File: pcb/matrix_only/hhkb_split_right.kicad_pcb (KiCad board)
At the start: 2 copper layers, 173.7 x 97.4 mm, 83 parts, among them SW1 CPG151101S11-2, SW10 CPG151101S11-2, SW11 CPG151101S11-2, SW12 CPG151101S11-2, SW13 CPG151101S11-2, SW14 CPG151101S11-2, SW15 CPG151101S11-2, SW16 CPG151101S11-2, SW17 CPG151101S11-2, SW18 CPG151101S11-2, SW19 CPG151101S11-2, SW2 CPG151101S11-2, SW20 CPG151101S11-2, SW21 CPG151101S11-2, SW22 CPG151101S11-2, SW23 CPG151101S11-2, SW24 CPG151101S11-2, SW25 CPG151101S11-2, SW26 CPG151101S11-2, SW27 CPG151101S11-2, SW28 CPG151101S11-2, SW29 CPG151101S11-2, SW3 CPG151101S11-2, SW30 CPG151101S11-2, SW31 CPG151101S11-2, SW32 CPG151101S11-2, SW33 CPG151101S11-2, SW34 CPG151101S11-2, SW4 CPG151101S11-2, SW5 CPG151101S11-2, SW6 CPG151101S11-2, SW7 CPG151101S11-2, SW8 CPG151101S11-2, SW9 CPG151101S11-2, U1 74LVC595, U2 74LVC595

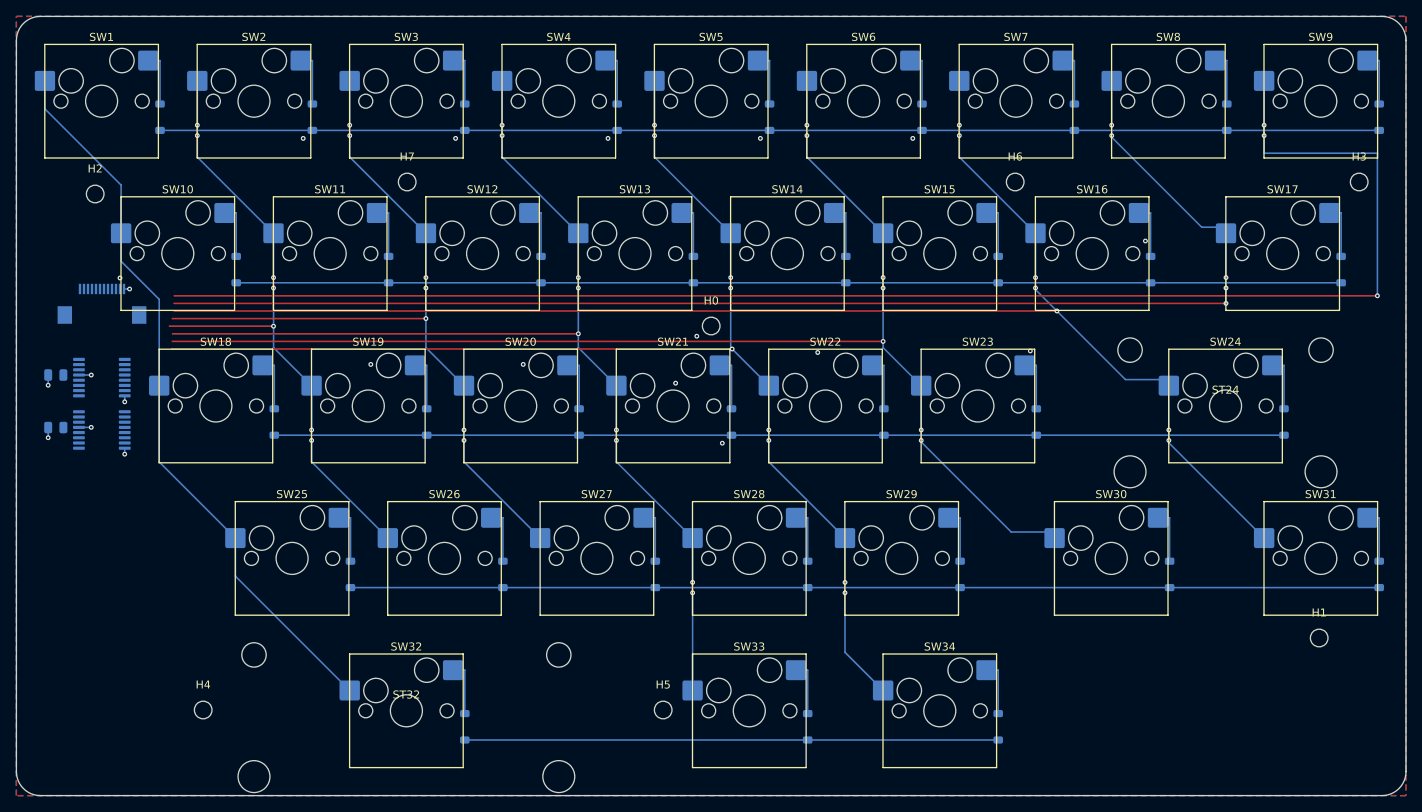
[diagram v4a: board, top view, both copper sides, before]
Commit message: 利用者が引いた配線を再現できるようにした（現物をスクリプト化）
利用者「**今の** matrix_only からスクリプト化すれば？」
「ただし、GND ベタ塗りとか、私が直せてないところは直してほしい」

## 仕組み

    tools/export_matrix_routing.py   pcb/matrix_only/ → pcb/matrix_routing.json
    tools/gen_pcb.py                 JSON を載せて pcb/unrouted/ へ

**規則として書き下すのではなく、現物の座標を写す。**私は規則を推測して
3 回失敗している（着地で U1 の他のパッドを横切る／レーンを縦に伸ばして
交差する／跨がない行に橋を架ける）。**利用者が引いた座標そのものが仕様。**

検証: 左 192 個・右 442 個が **0.002mm 以内で完全一致**（欠け 0）。

## 直したもの（利用者が直せていなかった部分）

1. **GND ベタが古かった。**`_pour` は配線を載せる前に走るので、あとから
   載る線を知らない。**最後に塗り直す**ようにした。
   `isolated_copper` 左 36 / 右 60 → **0**。離島も繋ぎ直した（左 9・右 16）。
2. **GND ビアが COL8 のレーンに乗っていた**（短絡 1・クリアランス 1）。
   `gnd_fanout.place` も配線より先に走るため。**当たるビアを外す処理**
   （`_drop_gnd_vias_hitting`）を足した。右 1 個 → 違反 0。

## 配置も取り込んだ

    U1   帯1 x=-62.787 dy=+1.375
    U2   帯1 x=-76.170 dy=+8.038 **角度 90**
    C_U1/C_U2  オフセットと**角度**（DECOUPLE_ANGLE を新設）

`_place_beside` は向きを自動で決めるが、利用者が IC を回した場合は
算出では出ないので、指定できるようにした。4 部品とも差 0.000mm。

## DRC

    左  違反 0 / 未配線 17（**左にはレーンが無い**——右だけ引かれている）
    右  dangling 9（レーン左端の余りと着地ビア）/ 未配線 **0**

短絡・交差・クリアランス・絶縁はすべて 0。

⚠️ **本番の pcb/ は触っていない**（利用者「まだ完成してないので、本番に
勝手にもっていかないでほしかった」）。

⚠️ `test_matrix_columns_do_not_need_long_crossings[right]` が新しく赤。
**利用者が引いたレーン（COL8 が 137.6mm の横断）を検出している。**
この検査は「列のバスに 27mm を超える区間があれば横断」と見るが、
**レーンは意図的な横断**なので前提が合わなくなった。別途直す。

Co-Authored-By: Claude Opus 5 (1M context) <noreply@anthropic.com>
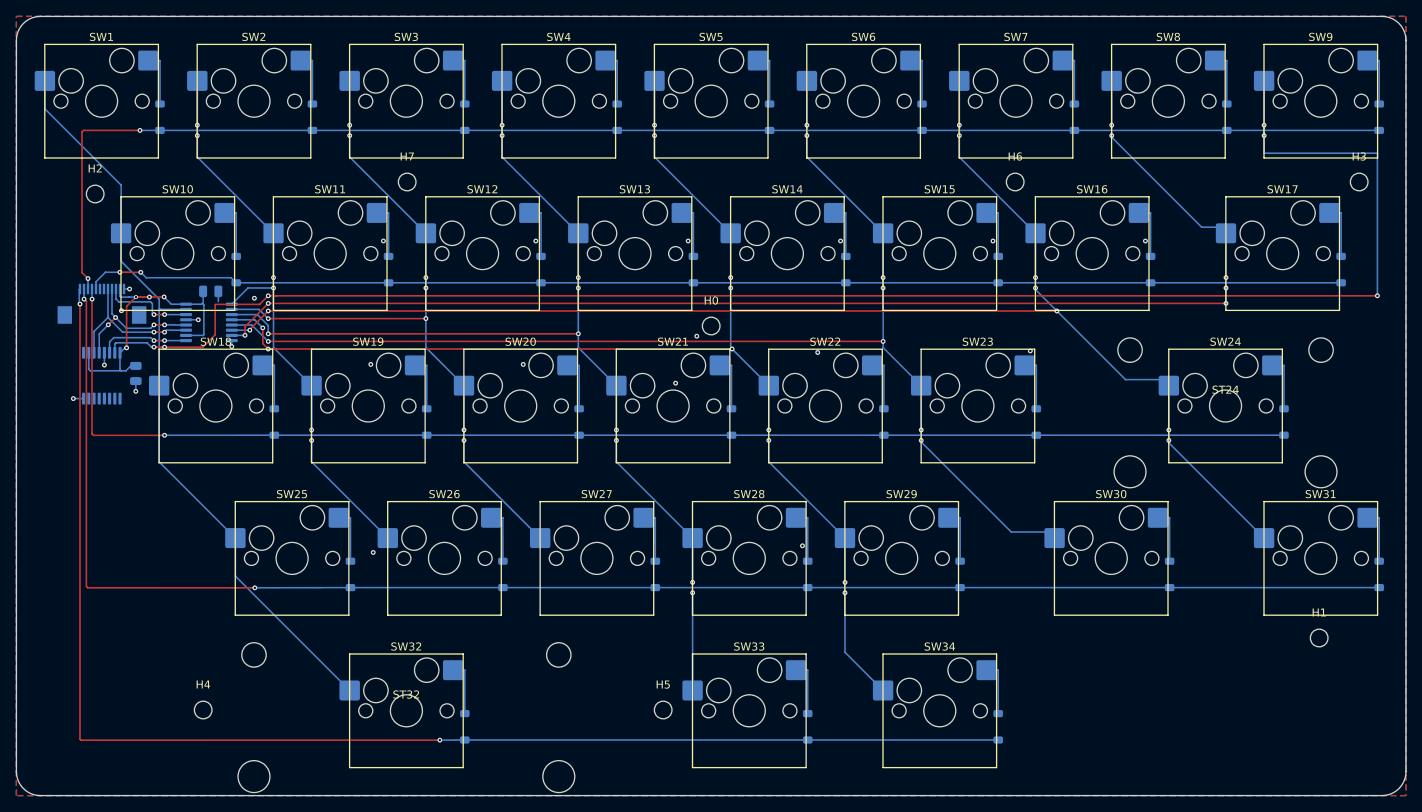
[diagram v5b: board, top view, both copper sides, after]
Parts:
- moved C_U1 22.0 mm to (87.4, 85.7), turned to 0 degrees
- moved U1 15.1 mm to (87.2, 89.5)
- moved C_U2 12.1 mm to (78.1, 95.9), turned to -90 degrees
- moved U2 6.78 mm to (73.8, 96.2), turned to 90 degrees
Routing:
- net ROW_E: track 66.7 -> 171.2 mm, vias 0 -> 2
- net ROW_D: track 128.6 -> 199.0 mm, vias 0 -> 2
- net ROW_B: track 126.2 -> 167.2 mm, vias 0 -> 2
- net V3V3: track 0.00 -> 39.7 mm, vias 1 -> 4
- net ROW_C: track 152.4 -> 182.2 mm, vias 0 -> 2
- net ROW_A: track 138.1 -> 157.7 mm, vias 0 -> 2
- net SPI_SCK: track 0.00 -> 19.3 mm, vias 0 -> 2
- net CS: track 0.00 -> 18.5 mm, vias 0 -> 4
- net COL8: track 191.4 -> 205.5 mm, vias 3 -> 6
- net SPI_MOSI: track 0.00 -> 11.6 mm, vias 0 -> 2
- net U1_U2: track 0.00 -> 11.3 mm, vias 0 -> 2
- net COL2: track 98.7 -> 91.8 mm, vias 7 -> 8
- net COL1: track 80.0 -> 73.1 mm, vias 7 -> 6
- net COL5: track 162.0 -> 155.4 mm, vias 7 -> 8
- net COL6: track 186.4 -> 180.3 mm, vias 7 -> 9
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
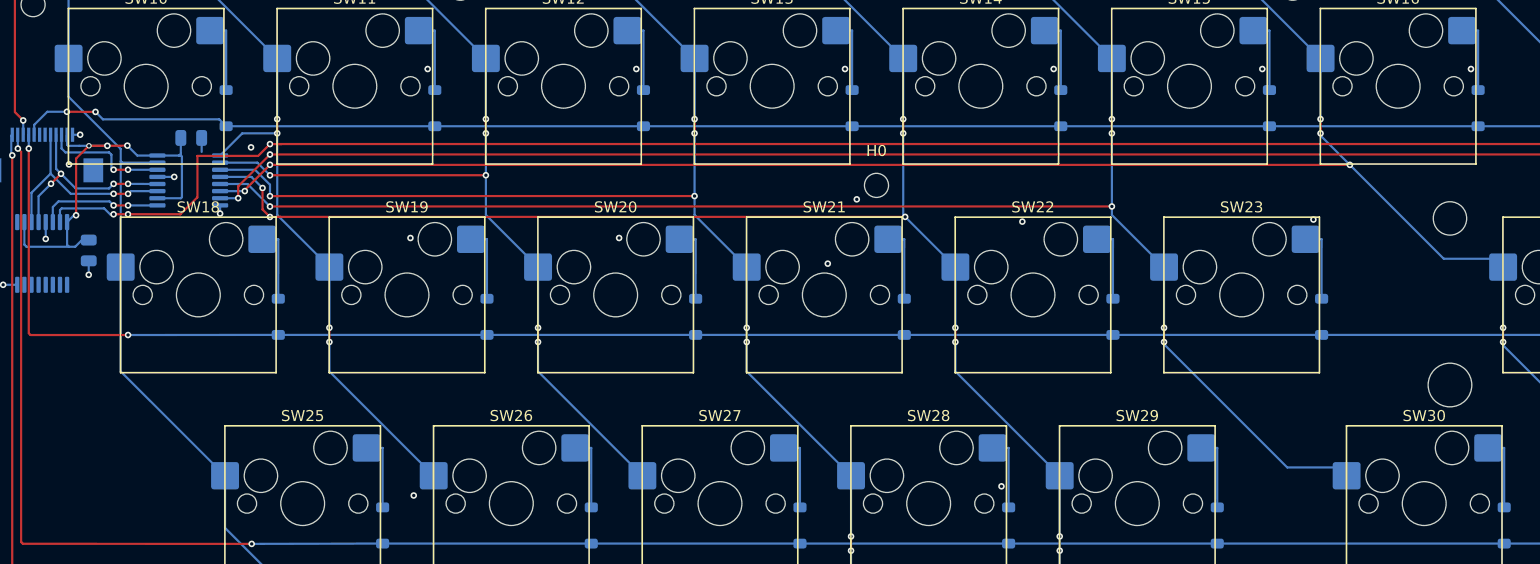
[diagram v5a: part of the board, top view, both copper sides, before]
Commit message: どこにも繋がっていない GND ビアを既定で打たなくした
利用者「どこにもつながってない GND ビアを一旦入れないようにしてほしいです。
それは最後にやる工程なはずなので。」

`gnd_fanout.stitch_islands` が打つ離島の縫い止めは、**ベタ以外の何にも
触れていない。**配線が動けばベタの形が変わり、要らなくなる／別の場所に
要る。**しかも浮いたビアはこれから引く配線の邪魔をする。**

→ **既定では打たない。**配線が固まってから最後に 1 回だけ:

    GND_STITCH=1 "$KPY" tools/gen_pcb.py

紛れ込んだ浮きビアを落とす `_drop_stitch_vias()` も足した。判定は
「GND のパッドにも GND の配線にも触れていないビア」。**`gnd_fanout.place`
のファンアウト（GND パッドの真横）は残る**——あれはパッドに繋がっている。

## 効いていることを数えた

ビアの総数（`(via` の行数）:

    左   既定 38  /  GND_STITCH=1  74   差 36
    右   既定 95  /  GND_STITCH=1 155   差 60

**この差が、これまで入っていた浮きビア。**「打たない設定にした」だけでは
効いた証拠にならないので、両方を出して数えた。

## 副作用が無いことを確かめた

利用者が引いた配線（pcb/matrix_routing.json）と照合:

    left:  配線 158 中 失った 0 / ビア 34 中 失った 0
    right: 配線 353 中 失った 0 / ビア 89 中 失った 0

⚠️ **これから DRC に `isolated_copper` が出る**（左 36 / 右 60 相当）。
縫っていないので出るのが正しい。**これを見て「壊れた」と思わないこと。**

⚠️ 本番の pcb/ は触っていない（pcb/unrouted/ と pcb/matrix_only/ のみ）。

Co-Authored-By: Claude Opus 5 (1M context) <noreply@anthropic.com>
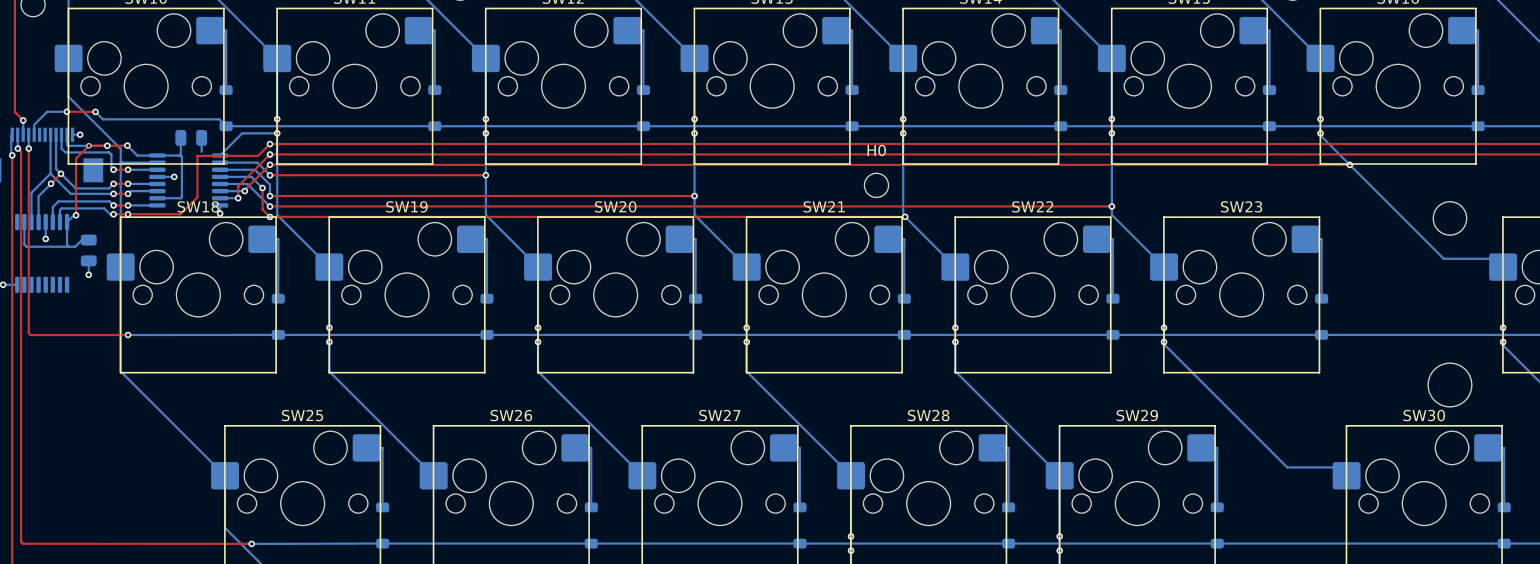
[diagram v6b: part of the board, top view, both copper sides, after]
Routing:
- net GND: vias 22 -> 6

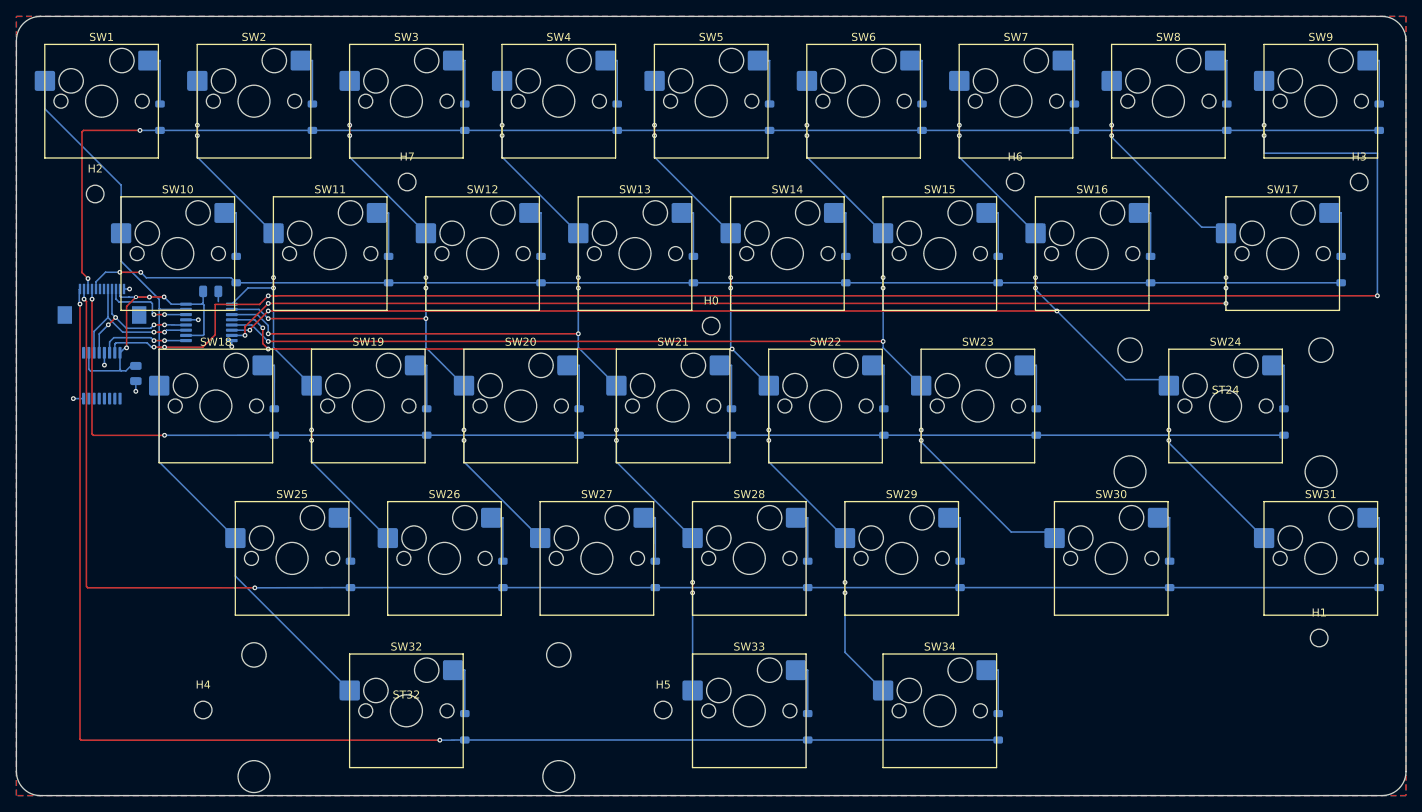
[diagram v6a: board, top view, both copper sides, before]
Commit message: 配線を塞いでいた取付穴 2 つを動かした（右 H0 / H2）
利用者「col 接続用の横ラインの途中に、基板の穴があります。非常に邪魔」
「1 行 1 列のところにある穴も、少し調節して、ROW0 への配線が綺麗になるように」

## なぜ塞いでいたか

**穴を決めたときの目的関数に「配線」が入っていなかった**（2026-08-12）。
当時は「キーから最寄りの留め点までの最大距離を小さくする」の 1 本だけで、
**横ライン（COL → U1/U2）はまだ存在しなかった。**あとから引いた線が
穴にぶつかった。**5 つ目の条件が増えた。**

    H0  (0.00, 10.00) → (0.00, 28.00)    配線まで 0.675 → 1.607mm
    H2  (-77.00, 26.50) → (-82.40, 26.50) 配線まで 0.460 → 2.540mm

**H0 は横ラインの帯（板 y=86.2..92.9）の真ん中に立っていた。**

**H2 は ROW0 の縦降りを挟んでいた。**⚠️ **ROW0 は `ROW_A` ではなく
`ROW_C`**（D1 の接続先で確かめた。名前と行番号は一致しない）。

## H0 は「規則」で選んだ。数字が最良だからではない

利用者に「H0 以外に、H0 と規則的に並んでいる穴があるんですか？」と
問われて調べたら、**H0 は他のどの穴とも x も y も揃っていなかった。**
「並びが崩れる」という私の反対理由は**誤りだった。**

**揃っているのは y=28 の 3 個**（H7 -38 / H6 38 / H3 81）で、
**x は -38 / 38 が 38mm 等間隔。その真ん中の x=0 が空席だった。**
銅までの隙間は (9.10, 29.00) の 2.36mm が最良だが、**規則に載る
(0.00, 28.00) を採った**（1.61mm でも帯から 14mm 外れる）。

## H2 は「縁」と「配線」の折り合い

⚠️ **この 2 つは真正面から競合する**（ROW_C の F.Cu 縦降りが板 x=71.34）。
一度 x=-84.65 まで逃がして配線 4.79mm を得たが、利用者「基板端すぎる」。
**縁 3.40mm を取って配線 2.54mm。**x=-79.90 まで戻すと配線 0.04mm で落ちる。

**どちらもキーからの最大距離 35.33mm を悪化させていない**（動かす前と同じ）。

## この移動で 1 件出た課題: 名札がキーの枠に重なっていた

H0 を動かしたら `silk_overlap` が 1 件増えた。**取付穴の名札は既定で
穴の 3.15mm 手前に出るが、そこはすぐ手前のキーの枠の中**だった。
**同じものが前から 4 件出ていた**（H1/H3/H6/H7）。警告なので誰も見ていない。
**5 件目を作って初めて 4 件に気づいた。**

→ `_place_hole_label` が手前・奥・左・右を試し、**当たらない向きへ回す。**
全部当たるなら既定のまま（**名札を消して黙らせない**。消すと穴が識別できない）。

    silk_overlap  右 13 → 9 ／ 左 7 → 3（取付穴がらみは 0）

⚠️ **故意に壊して確かめた。**逃がし先を 1 方向だけにすると DRC が 5 件出す。

## 測ったこと

    DRC 前後差       増えた違反 0 件 ／ 消えた 4 件
    利用者の配線     左 158+34 ・右 353+89  失った 0
    柱 φ4 と全 73 部品のコートヤード  8 本とも当たらない（最小 2.655mm）
    プレートの STL   新 8 か所に柱 ／ **旧 2 か所は頂点 0**（残っていない）
    組み立て STL     平らな板と x の値の集合が完全一致・柱の頂点数も全一致

CAD の生成物も出し直した（STL・build/plate_*.stl・.blend）。
⚠️ **refresh_view.sh は build/plate_*.stl を出さない。**放っておくと
8/17 のまま残る（実際に古い位置の柱が入っていた）。gen_plate.py を別に叩く。

## 検査

**16 件赤。うち 15 件は自分より前から赤**（git stash して確認）。
残る 1 件 `test_the_pcb_is_actually_fastened_to_the_plate[right]` は
「H0 に ic_tssop16 が当た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
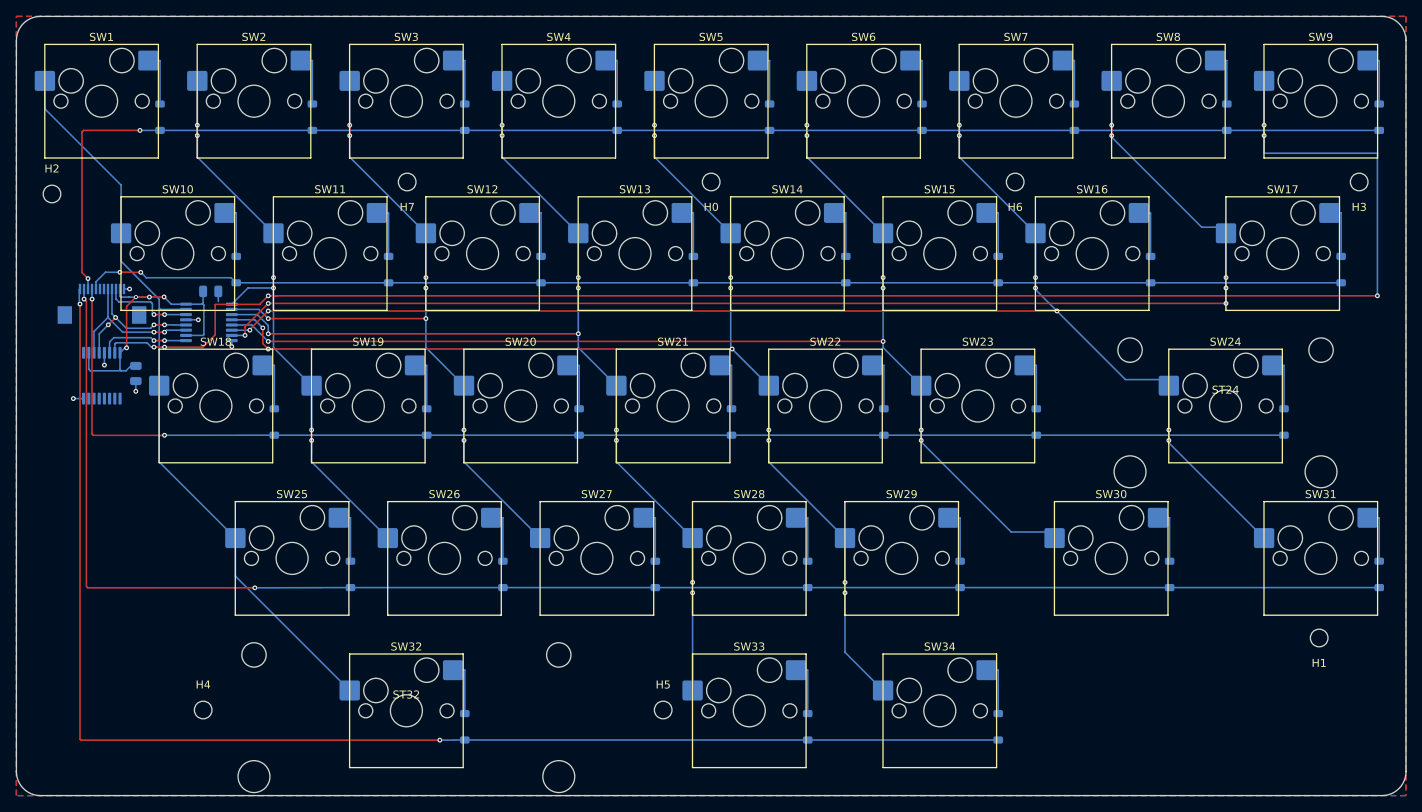
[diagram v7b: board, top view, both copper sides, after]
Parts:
- moved H0 18.0 mm to (150.0, 72.0)
- moved H2 5.40 mm to (67.6, 73.5)
